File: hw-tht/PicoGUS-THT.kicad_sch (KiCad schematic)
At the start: 39 parts, among them J1 IRQDMA_JP, J2 ISA debug (DNP), J3 Bus_ISA_8bit, J5 SJ1-3535NG, J6 UART_TX, J7 USB power jumper, U1 Pico, U10 74AHCT126, U2 74AHC244, U3 SN74CB3T3257, U4 SN74CB3T3257, U5 74AHC14, U6 74AHC00, U7 74AHC00, U8 APS6404L-3SQR-SN

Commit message: hw-tht: v1.3.0, axial/0805 hybrid resistors, decoupling placement
- Board revision v1.3.0 (schematic title blocks and README); take over
  the reviewed layout including the rotated PicoGUS logo and the new
  version and credit texts. The review board is now the build base, so
  its artwork is kept as drawn.
- New R_Axial_DIN0207_P10.16mm_0805_Hybrid footprint (0805 pads between
  the axial holes) for all resistors; BOM lists Yageo RC0805 (DigiKey)
  and UNI-ROYAL 0805W8F (LCSC) alternatives.
- Decoupling back next to the pins it serves, as on v1.2: DAC caps at
  CPVDD/CAPP-CAPM/VNEG/AVDD/DVDD, C4 at U2, C10 at the PSRAM, C3/C5 on
  the supply side of U3/U4. MIDI resistors and ferrites in one row
  next to J5, DAC output filters below the DAC.

Co-Authored-By: Claude Opus 5.5 <noreply@anthropic.com>
Claude-Session: https://claude.ai/code/session_011utN3x8yYUNDvkpGCEq5yD
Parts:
- R1: footprint Resistor_THT:R_Axial_DIN0207_L6.3mm_D2.5mm_P10.16mm_Horizontal -> PicoGUS-THT:R_Axial_DIN0207_P10.16mm_0805_Hybrid; Alternatives (none) -> 0805 SMD (fits between the holes): Yageo RC0805FR-071KL (DK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
- R17: footprint Resistor_THT:R_Axial_DIN0207_L6.3mm_D2.5mm_P10.16mm_Horizontal -> PicoGUS-THT:R_Axial_DIN0207_P10.16mm_0805_Hybrid; Alternatives (none) -> 0805 SMD (fits between the holes): Yageo RC0805FR-0710KL (D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
- R18: footprint Resistor_THT:R_Axial_DIN0207_L6.3mm_D2.5mm_P10.16mm_Horizontal -> PicoGUS-THT:R_Axial_DIN0207_P10.16mm_0805_Hybrid; Alternatives (none) -> 0805 SMD (fits between the holes): Yageo RC0805FR-07100KL (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
- R2, R5, R6: footprint Resistor_THT:R_Axial_DIN0207_L6.3mm_D2.5mm_P10.16mm_Horizontal -> PicoGUS-THT:R_Axial_DIN0207_P10.16mm_0805_Hybrid; Alternatives (none) -> 0805 SMD (fits between the holes): Yageo RC0805FR-0715KL (D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
- R3, R4: footprint Resistor_THT:R_Axial_DIN0207_L6.3mm_D2.5mm_P10.16mm_Horizontal -> PicoGUS-THT:R_Axial_DIN0207_P10.16mm_0805_Hybrid; Alternatives (none) -> 0805 SMD (fits between the holes): Yageo RC0805FR-07220RL (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
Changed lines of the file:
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@@
 		(title "PicoGUS THT")
 		(date "2026-09-28")
-		(rev "v1.2-THT")
+		(rev "v1.3.0")
 		(comment 1 "Through-hole variant of PicoGUS v1.2 with Waveblaster header")
 		(comment 2 "DIP logic footprints also accept a TSSOP (hybrid footprints)")
@@
 			)
 		)
-		(property "Footprint" "Resistor_THT:R_Axial_DIN0207_L6.3mm_D2.5mm_P10.16mm_Horizontal"
+		(property "Footprint" "PicoGUS-THT:R_Axial_DIN0207_P10.16mm_0805_Hybrid"
 			(at 240.792 144.145 90)
 			(hide yes)
@@
 			)
 		)
+		(property "Alternatives" "0805 SMD (fits between the holes): Yageo RC0805FR-071KL (DK 311-1.00KCRCT-ND, 732526), UNI-ROYAL 0805W8F (LCSC C17513, 26812400)."
+			(at 242.57 144.145 0)
+			(hide yes)
+			(effects
+				(font
+					(size 1.27 1.27)
+				)
+				(hide yes)
+			)
+		)
 		(pin "1"
 		)
@@
 			)
 		)
-		(property "Footprint" "Resistor_THT:R_Axial_DIN0207_L6.3mm_D2.5mm_P10.16mm_Horizontal"
+		(property "Footprint" "PicoGUS-THT:R_Axial_DIN0207_P10.16mm_0805_Hybrid"
 			(at 266.192 144.145 90)
 			(hide yes)
@@
 			)
 		)
+		(property "Alternatives" "0805 SMD (fits between the holes): Yageo RC0805FR-0715KL (DK 311-15.0KCRCT-ND, 127426), UNI-ROYAL 0805W8F (LCSC C17475, 524100)."
+			(at 267.97 144.145 0)
+			(hide yes)
+			(effects
+				(font
+					(size 1.27 1.27)
+				)
+				(hide yes)
+			)
+		)
 		(pin "1"
 		)
@@
 			)
 		)
-		(property "Footprint" "Resistor_THT:R_Axial_DIN0207_L6.3mm_D2.5mm_P10.16mm_Horizontal"
+		(property "Footprint" "PicoGUS-THT:R_Axial_DIN0207_P10.16mm_0805_Hybrid"
 			(at 232.918 56.515 90)
 			(hide yes)
@@
 			)
 		)
+		(property "Alternatives" "0805 SMD (fits between the holes): Yageo RC0805FR-07220RL (DK 311-220CRCT-ND, 420320), UNI-ROYAL 0805W8F (LCSC C17557, 569300)."
+			(at 231.14 56.515 0)
+			(hide yes)
+			(effects
+				(font
+					(size 1.27 1.27)
+				)
+				(hide yes)
+			)
+		)
 		(pin "1"
 		)
@@
 			)
 		)
-		(property "Footprint" "Resistor_THT:R_Axial_DIN0207_L6.3mm_D2.5mm_P10.16mm_Horizontal"
+		(property "Footprint" "PicoGUS-THT:R_Axial_DIN0207_P10.16mm_0805_Hybrid"
 			(at 224.79 72.263 90)
 			(hide yes)
@@
 			)
 		)
+		(property "Alternatives" "0805 SMD (fits between the holes): Yageo RC0805FR-07220RL (DK 311-220CRCT-ND, 420320), UNI-ROYAL 0805W8F (LCSC C17557, 569300)."
+			(at 224.79 70.485 0)
+			(hide yes)
+			(effects
+				(font
+					(size 1.27 1.27)
+				)
+				(hide yes)
+			)
+		)
 		(pin "1"
 		)
@@
 			)
 		)
-		(property "Footprint" "Resistor_THT:R_Axial_DIN0207_L6.3mm_D2.5mm_P10.16mm_Horizontal"
+		(property "Footprint" "PicoGUS-THT:R_Axial_DIN0207_P10.16mm_0805_Hybrid"
 			(at 219.837 155.575 90)
 			(hide yes)
@@
 			)
 		)
+		(property "Alternatives" "0805 SMD (fits between the holes): Yageo RC0805FR-0715KL (DK 311-15.0KCRCT-ND, 127426), UNI-ROYAL 0805W8F (LCSC C17475, 524100)."
+			(at 221.615 155.575 0)
+			(hide yes)
+			(effects
+				(font
+					(size 1.27 1.27)
+				)
+				(hide yes)
+			)
+		)
 		(pin "1"
 		)
@@
 			)
 		)
-		(property "Footprint" "Resistor_THT:R_Axial_DIN0207_L6.3mm_D2.5mm_P10.16mm_Horizontal"
+		(property "Footprint" "PicoGUS-THT:R_Axial_DIN0207_P10.16mm_0805_Hybrid"
 			(at 162.687 121.92 90)
 			(hide yes)
@@
 			)
 		)
+		(property "Alternatives" "0805 SMD (fits between the holes): Yageo RC0805FR-0715KL (DK 311-15.0KCRCT-ND, 127426), UNI-ROYAL 0805W8F (LCSC C17475, 524100)."
+			(at 164.465 121.92 0)
+			(hide yes)
+			(effects
+				(font
+					(size 1.27 1.27)
+				)
+				(hide yes)
+			)
+		)
 		(pin "1"
 		)
@@
 			)
 		)
-		(property "Footprint" "Resistor_THT:R_Axial_DIN0207_L6.3mm_D2.5mm_P10.16mm_Horizontal"
+		(property "Footprint" "PicoGUS-THT:R_Axial_DIN0207_P10.16mm_0805_Hybrid"
 			(at 280.67 30.48 0)
 			(hide yes)
@@
 			)
 		)
+		(property "Alternatives" "0805 SMD (fits between the holes): Yageo RC0805FR-0710KL (DK 311-10.0KCRCT-ND, 2120333), UNI-ROYAL 0805W8F (LCSC C17414, 43352900)."
+			(at 280.67 30.48 0)
+			(hide yes)
+			(show_name no)
+			(do_not_autoplace no)
+			(effects
+				(font
+					(size 1.27 1.27)
+				)
+			)
+		)
 		(property "LCSC" "C1519255"
 			(at 280.67 30.48 0)
@@
 			)
 		)
-		(property "Footprint" "Resistor_THT:R_Axial_DIN0207_L6.3mm_D2.5mm_P10.16mm_Horizontal"
+		(property "Footprint" "PicoGUS-THT:R_Axial_DIN0207_P10.16mm_0805_Hybrid"
 			(at 210.82 152.4 0)
 			(hide yes)
@@
 			(at 210.82 152.4 0)
 			(hide yes)
+			(show_name no)
+			(do_not_autoplace no)
+			(effects
+				(font
+					(size 1.27 1.27)
+				)
+			)
+		)
+		(property "Alternatives" "0805 SMD (fits between the holes): Yageo RC0805FR-07100KL (DK 311-100KCRCT-ND, 1068493), UNI-ROYAL 0805W8F (LCSC C149504, 3119100)."
+			(at 210.82 152.4 0)
+			(hide yes)

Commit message: hw-tht: 5 mm disc/0805 hybrid capacitors, labels inside or beside bodies
- New C_Disc_D5.0mm_W2.5mm_P5.00mm_0805_Hybrid footprint for all ceramic
  caps: 5.0/5.08 mm radial part OR an 0805 between the holes. Replaces
  the 2.5/5.0 mm dual-pitch footprint.
- BOM: every ceramic cap line is now 5 mm pitch at both distributors
  (2.2 nF LCSC Dersonic C22391154, 100 pF DigiKey Vishay
  K101J15C0GF5TH5) and lists an in-stock 0805 alternative.
- Silkscreen labels: FB1/FB2 inside the body like the resistors;
  capacitor labels just outside the body, above/left, else at a free end.

Co-Authored-By: Claude Opus 5.5 <noreply@anthropic.com>
Claude-Session: https://claude.ai/code/session_011utN3x8yYUNDvkpGCEq5yD
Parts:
- C10: footprint PicoGUS-THT:C_Disc_D5.0mm_W2.5mm_P2.50mm_P5.00mm -> PicoGUS-THT:C_Disc_D5.0mm_W2.5mm_P5.00mm_0805_Hybrid; Alternatives (none) -> 0805 SMD: Yageo CC0805KKX7R9BB105 (DK 311-1886-1-ND, 82107;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
- C11, C3, C4, C5, C6, C7, C8, C9: footprint PicoGUS-THT:C_Disc_D5.0mm_W2.5mm_P2.50mm_P5.00mm -> PicoGUS-THT:C_Disc_D5.0mm_W2.5mm_P5.00mm_0805_Hybrid; Alternatives (none) -> 0805 SMD (fits between the holes): Samsung CL21B104KBCNNNC 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
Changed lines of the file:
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@@
 			)
 		)
-		(property "Footprint" "PicoGUS-THT:C_Disc_D5.0mm_W2.5mm_P2.50mm_P5.00mm"
+		(property "Footprint" "PicoGUS-THT:C_Disc_D5.0mm_W2.5mm_P5.00mm_0805_Hybrid"
 			(at 63.8302 190.5 0)
 			(hide yes)
@@
 			)
 		)
+		(property "Alternatives" "0805 SMD: Yageo CC0805KKX7R9BB105 (DK 311-1886-1-ND, 82107; LCSC C91185, 809080)."
+			(at 62.865 186.69 0)
+			(hide yes)
+			(effects
+				(font
+					(size 1.27 1.27)
+				)
+				(hide yes)
+			)
+		)
 		(pin "1"
 		)
@@
 			)
 		)
-		(property "Footprint" "PicoGUS-THT:C_Disc_D5.0mm_W2.5mm_P2.50mm_P5.00mm"
+		(property "Footprint" "PicoGUS-THT:C_Disc_D5.0mm_W2.5mm_P5.00mm_0805_Hybrid"
 			(at 53.6702 190.5 0)
 			(hide yes)
@@
 			)
 		)
+		(property "Alternatives" "0805 SMD (fits between the holes): Samsung CL21B104KBCNNNC (DK 1276-1003-1-ND, 4889645; LCSC C1711, 1029920)."
+			(at 52.705 186.69 0)
+			(hide yes)
+			(effects
+				(font
+					(size 1.27 1.27)
+				)
+				(hide yes)
+			)
+		)
 		(pin "1"
 		)
@@
 			)
 		)
-		(property "Footprint" "PicoGUS-THT:C_Disc_D5.0mm_W2.5mm_P2.50mm_P5.00mm"
+		(property "Footprint" "PicoGUS-THT:C_Disc_D5.0mm_W2.5mm_P5.00mm_0805_Hybrid"
 			(at 28.2702 190.5 0)
 			(hide yes)
@@
 			)
 		)
+		(property "Alternatives" "0805 SMD (fits between the holes): Samsung CL21B104KBCNNNC (DK 1276-1003-1-ND, 4889645; LCSC C1711, 1029920)."
+			(at 27.305 186.69 0)
+			(hide yes)
+			(effects
+				(font
+					(size 1.27 1.27)
+				)
+				(hide yes)
+			)
+		)
 		(pin "1"
 		)
@@
 			)
 		)
-		(property "Footprint" "PicoGUS-THT:C_Disc_D5.0mm_W2.5mm_P2.50mm_P5.00mm"
+		(property "Footprint" "PicoGUS-THT:C_Disc_D5.0mm_W2.5mm_P5.00mm_0805_Hybrid"
 			(at 33.3502 190.5 0)
 			(hide yes)
@@
 			)
 		)
+		(property "Alternatives" "0805 SMD (fits between the holes): Samsung CL21B104KBCNNNC (DK 1276-1003-1-ND, 4889645; LCSC C1711, 1029920)."
+			(at 32.385 186.69 0)
+			(hide yes)
+			(effects
+				(font
+					(size 1.27 1.27)
+				)
+				(hide yes)
+			)
+		)
 		(pin "1"
 		)
@@
 			)
 		)
-		(property "Footprint" "PicoGUS-THT:C_Disc_D5.0mm_W2.5mm_P2.50mm_P5.00mm"
+		(property "Footprint" "PicoGUS-THT:C_Disc_D5.0mm_W2.5mm_P5.00mm_0805_Hybrid"
 			(at 243.5352 159.385 0)
 			(hide yes)
@@
 			)
 		)
+		(property "Alternatives" "0805 SMD (fits between the holes): Samsung CL21B104KBCNNNC (DK 1276-1003-1-ND, 4889645; LCSC C1711, 1029920)."
+			(at 242.57 155.575 0)
+			(hide yes)
+			(effects
+				(font
+					(size 1.27 1.27)
+				)
+				(hide yes)
+			)
+		)
 		(pin "1"
 		)
@@
 			)
 		)
-		(property "Footprint" "PicoGUS-THT:C_Disc_D5.0mm_W2.5mm_P2.50mm_P5.00mm"
+		(property "Footprint" "PicoGUS-THT:C_Disc_D5.0mm_W2.5mm_P5.00mm_0805_Hybrid"
 			(at 58.7502 190.5 0)
 			(hide yes)
@@
 			)
 		)
+		(property "Alternatives" "0805 SMD (fits between the holes): Samsung CL21B104KBCNNNC (DK 1276-1003-1-ND, 4889645; LCSC C1711, 1029920)."
+			(at 57.785 186.69 0)
+			(hide yes)
+			(effects
+				(font
+					(size 1.27 1.27)
+				)
+				(hide yes)
+			)
+		)
 		(pin "1"
 		)
@@
 			)
 		)
-		(property "Footprint" "PicoGUS-THT:C_Disc_D5.0mm_W2.5mm_P2.50mm_P5.00mm"
+		(property "Footprint" "PicoGUS-THT:C_Disc_D5.0mm_W2.5mm_P5.00mm_0805_Hybrid"
 			(at 43.5102 190.5 0)
 			(hide yes)
@@
 			)
 		)
+		(property "Alternatives" "0805 SMD (fits between the holes): Samsung CL21B104KBCNNNC (DK 1276-1003-1-ND, 4889645; LCSC C1711, 1029920)."
+			(at 42.545 186.69 0)
+			(hide yes)
+			(effects
+				(font
+					(size 1.27 1.27)
+				)
+				(hide yes)
+			)
+		)
 		(pin "1"
 		)
@@
 			)
 		)
-		(property "Footprint" "PicoGUS-THT:C_Disc_D5.0mm_W2.5mm_P2.50mm_P5.00mm"
+		(property "Footprint" "PicoGUS-THT:C_Disc_D5.0mm_W2.5mm_P5.00mm_0805_Hybrid"
 			(at 48.5902 190.5 0)
 			(hide yes)
@@
 			)
 		)
+		(property "Alternatives" "0805 SMD (fits between the holes): Samsung CL21B104KBCNNNC (DK 1276-1003-1-ND, 4889645; LCSC C1711, 1029920)."
+			(at 47.625 186.69 0)
+			(hide yes)
+			(effects
+				(font
+					(size 1.27 1.27)
+				)
+				(hide yes)
+			)
+		)
 		(pin "1"
 		)
@@
 			)
 		)
-		(property "Footprint" "PicoGUS-THT:C_Disc_D5.0mm_W2.5mm_P2.50mm_P5.00mm"
+		(property "Footprint" "PicoGUS-THT:C_Disc_D5.0mm_W2.5mm_P5.00mm_0805_Hybrid"
 			(at 38.4302 190.5 0)
 			(hide yes)
@@
 			(at 37.465 186.69 0)
 			(hide yes)
+			(effects
+				(font
+					(size 1.27 1.27)
+				)
+				(hide yes)
+			)
+		)
+		(property "Alternatives" "0805 SMD (fits between the holes): Samsung CL21B104KBCNNNC (DK 1276-1003-1-ND, 4889645; LCSC C1711, 1029920)."
+			(at 37.465 186.69 0)
+			(hide yes)

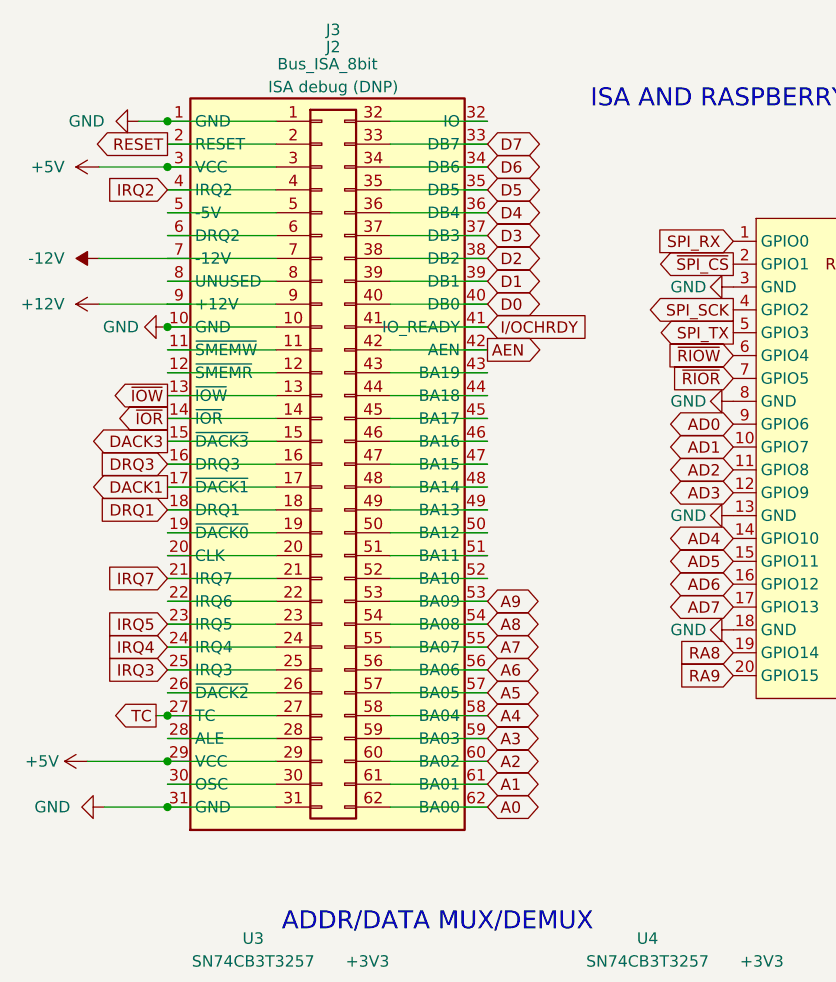
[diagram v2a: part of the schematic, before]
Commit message: hw-tht: remove the J2 ISA debug header, move U3/U4 to the gold fingers
- J2 (2x31 ISA probe header, never fitted, carried over from v1.2) is
  removed from schematic, board and BOM. Its 62 pads formed a wall just
  above the fingers that every ISA signal had to cross, which kept the
  autorouter stuck. ISA pins that only went to J2 get no-connect flags.
- U3/U4 (CB3T3257 bus switches) sit in the freed strip right above the
  data-line fingers, with C3/C5 2.5 mm from their supply pins; their 16
  ISA-side lines are now short, only the 8 AD lines run to the Pico.
- Power tracks: +5V/+3V3/VSYS 0.4 mm (was 0.5 mm, barely fit between
  DIP pins); +/-12V use normal 0.25 mm tracks (a few mA).

Co-Authored-By: Claude Opus 5.5 <noreply@anthropic.com>
Claude-Session: https://claude.ai/code/session_011utN3x8yYUNDvkpGCEq5yD
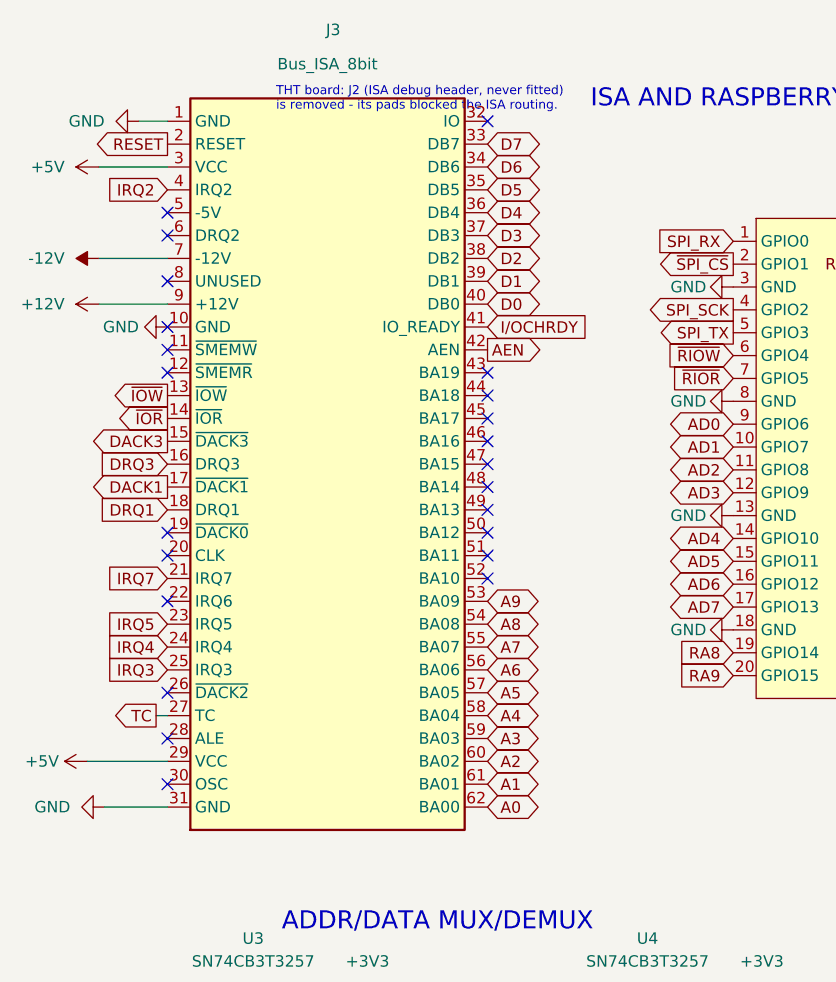
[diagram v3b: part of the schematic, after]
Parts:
- removed J2: ISA debug (DNP), Connector_PinHeader_2.54mm:PinHeader_2x31_P2.54mm_Vertical, symbol Connector_Generic:Conn_02x31_Top_Bottom
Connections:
- no-connect marks 9 -> 32
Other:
- note added: "THT board: J2 (ISA debug header, never fitted) is removed - its pads blocked the ISA routing."

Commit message: hw-tht: through-hole parts only, drop the hybrid footprints
- Resistors: plain axial DIN0207 (10.16 mm); ceramic caps: plain 5 mm
  disc; FB1/FB2: axial bead on leads (12.7 mm, Fair-Rite 2743002112 /
  LCSC FH RH3.5x0.8x9P52E); logic ICs: plain DIP-14/DIP-20.
- Only the parts that have no THT version stay SMD: U3/U4 (CB3T3257),
  U8 (APS6404L PSRAM), U9 (PCM510x DAC).
- BOM: 0805/TSSOP alternatives removed. The DIP logic ICs are DigiKey
  parts; LCSC has almost none in stock (listed with their real stock).
- Placement from the latest layout review (DIPs in one column, DAC and
  its caps next to the bus switches), FB1/FB2 and C19/C20 shifted to fit
  the longer bead footprint. Passive labels centred inside the bodies.

Co-Authored-By: Claude Opus 5.5 <noreply@anthropic.com>
Claude-Session: https://claude.ai/code/session_011utN3x8yYUNDvkpGCEq5yD
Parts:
- C10: footprint PicoGUS-THT:C_Disc_D5.0mm_W2.5mm_P5.00mm_0805_Hybrid -> Capacitor_THT:C_Disc_D5.0mm_W2.5mm_P5.00mm; Alternatives 0805 SMD: Yageo CC0805KKX7R9BB105 (DK 311-1886-1-ND, 82107;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 -> (none)
- C11, C3, C4, C5, C6, C7, C8, C9: footprint PicoGUS-THT:C_Disc_D5.0mm_W2.5mm_P5.00mm_0805_Hybrid -> Capacitor_THT:C_Disc_D5.0mm_W2.5mm_P5.00mm; Alternatives 0805 SMD (fits between the holes): Samsung CL21B104KBCNNNC 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 -> (none)
- FB1, FB2: value 1k@100MHz -> Ferrite bead; footprint PicoGUS-THT:FerriteBead_Axial_P10.16mm_0805_Hybrid -> Resistor_THT:R_Axial_DIN0309_L9.0mm_D3.2mm_P12.70mm_Horizontal; Alternatives (none) -> Fair-Rite 2761001112 (DK 1934-1423-1-ND, 33346). A wire lin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; DigiKey 490-1041-1-ND -> 1934-1477-1-ND; LCSC C85835 -> C192455 (FH RH3.5x0.8x9P52E (100R@100MHz)); MPN BLM21AG102SN1D -> 2743002112; Manufacturer Murata -> Fair-Rite
- R1: footprint PicoGUS-THT:R_Axial_DIN0207_P10.16mm_0805_Hybrid -> Resistor_THT:R_Axial_DIN0207_L6.3mm_D2.5mm_P10.16mm_Horizontal; Alternatives 0805 SMD (fits between the holes): Yageo RC0805FR-071KL (DK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 -> (none)
- R17: footprint PicoGUS-THT:R_Axial_DIN0207_P10.16mm_0805_Hybrid -> Resistor_THT:R_Axial_DIN0207_L6.3mm_D2.5mm_P10.16mm_Horizontal; Alternatives 0805 SMD (fits between the holes): Yageo RC0805FR-0710KL (D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 -> (none)
- R18: footprint PicoGUS-THT:R_Axial_DIN0207_P10.16mm_0805_Hybrid -> Resistor_THT:R_Axial_DIN0207_L6.3mm_D2.5mm_P10.16mm_Horizontal; Alternatives 0805 SMD (fits between the holes): Yageo RC0805FR-07100KL (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 -> (none)
- R2, R5, R6: footprint PicoGUS-THT:R_Axial_DIN0207_P10.16mm_0805_Hybrid -> Resistor_THT:R_Axial_DIN0207_L6.3mm_D2.5mm_P10.16mm_Horizontal; Alternatives 0805 SMD (fits between the holes): Yageo RC0805FR-0715KL (D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 -> (none)
- R3, R4: footprint PicoGUS-THT:R_Axial_DIN0207_P10.16mm_0805_Hybrid -> Resistor_THT:R_Axial_DIN0207_L6.3mm_D2.5mm_P10.16mm_Horizontal; Alternatives 0805 SMD (fits between the holes): Yageo RC0805FR-07220RL (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 -> (none)
- U10: footprint PicoGUS-THT:DIP-14_W7.62mm_TSSOP-14_Hybrid -> Package_DIP:DIP-14_W7.62mm; Alternatives DIP also as Rochester 2156-SN74AHCT126N-ND (58265). DigiKey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 -> Rochester 2156-SN74AHCT126N-ND (58265).; LCSC C155177 (SN74AHCT126PWR (TSSOP-14, fits inside the DIP)) -> C1548378
- U2: footprint PicoGUS-THT:DIP-20_W7.62mm_TSSOP-20_Hybrid -> Package_DIP:DIP-20_W7.62mm; Alternatives DIP also as Rochester 2156-SN74AHC244N-ND (9380). TSSOP at 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 -> Rochester 2156-SN74AHC244N-ND (9380).; LCSC C7668 (SN74LVC244APWR (TSSOP-20, fits the pads beside the D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 -> C1548228
- U5: footprint PicoGUS-THT:DIP-14_W7.62mm_TSSOP-14_Hybrid -> Package_DIP:DIP-14_W7.62mm; Alternatives LCSC 74AHC14PW,118 C138310 (4075); DigiKey TSSOP 74AHC14PW,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 -> (none); LCSC C7460 (SN74AHC14PWR (TSSOP-14, fits inside the DIP)) -> C2879116
- U6, U7: footprint PicoGUS-THT:DIP-14_W7.62mm_TSSOP-14_Hybrid -> Package_DIP:DIP-14_W7.62mm; Alternatives DIP also as Rochester 2156-SN74AHC00N-ND (21358). DigiKey T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 -> Rochester 2156-SN74AHC00N-ND (21358).; LCSC C7803 (SN74LVC00APWR (TSSOP-14, fits inside the DIP)) -> C2879122
